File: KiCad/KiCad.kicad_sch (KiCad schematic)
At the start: 48 parts, among them J1 DC-IN, J2 TYPE-C, J3 Conn_01x03_Pin, J4 Conn_01x03_Pin, J5 Conn_01x03_Pin, J6 Conn_01x03_Pin, Q1 IRF3708, SW1 reset, SW2 start, U1 ESP32-WROOM-32E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

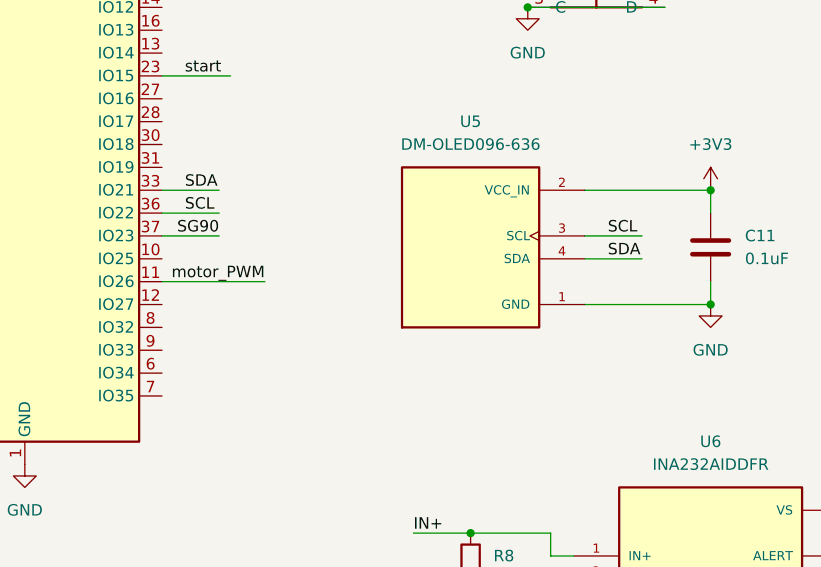
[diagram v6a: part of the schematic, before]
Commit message: 修改iic走線，將原本共用同一組iic的裝置分別接到兩不同的iic
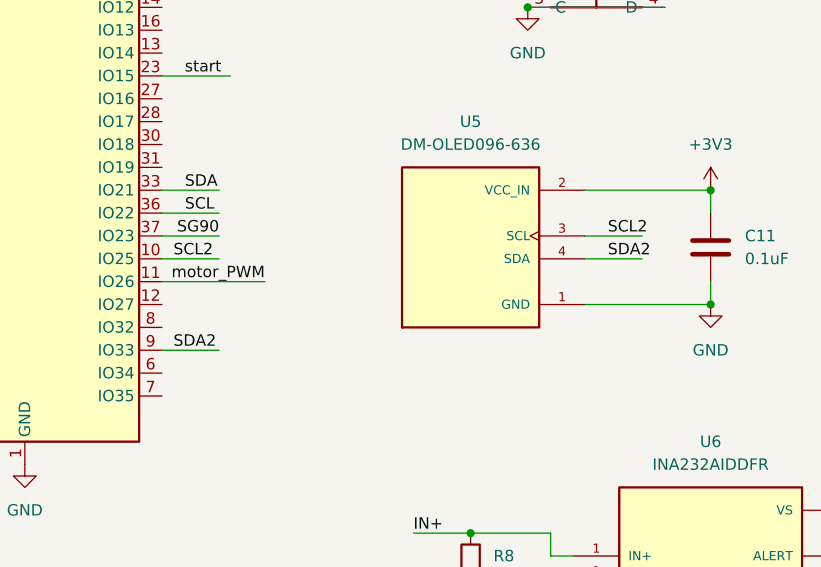
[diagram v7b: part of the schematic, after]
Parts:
- added unit 1 of U8
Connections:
- net SCL: no longer U5.3 (SCL)
- net SDA: no longer U5.4 (SDA)
- net at J6.2 (Pin_2): now also U8.1; no longer U8.1
- net at C17.1, R10.2: now also U8.2 (-), U8.3 (+); no longer U8.2 (-), U8.3 (+)
- net SCL2: now reaches U1.10 (IO25)
- net SCL2: now also U5.3 (SCL)
- net SDA2: now reaches U1.9 (IO33)
- net SDA2: now also U5.4 (SDA)
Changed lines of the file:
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@@
+	(wire
+		(pts
+			(xy 72.39 71.12) (xy 78.74 71.12)
+		)
+		(stroke
+			(width 0)
+			(type default)
+		)
+	)
 	(wire
 		(pts
@@
 	(wire
 		(pts
+			(xy 72.39 81.28) (xy 78.74 81.28)
+		)
+		(stroke
+			(width 0)
+			(type default)
+		)
+	)
+	(wire
+		(pts
 			(xy 261.62 26.67) (xy 266.7 26.67)
 		)
@@
 			(width 0)
 			(type default)
+		)
+	)
+	(label "SDA2"
+		(at 73.66 81.28 0)
+		(effects
+			(font
+				(size 1.27 1.27)
+			)
+			(justify left bottom)
 		)
 	)
@@
 		)
 	)
+	(label "SCL2"
+		(at 73.66 71.12 0)
+		(effects
+			(font
+				(size 1.27 1.27)
+			)
+			(justify left bottom)
+		)
+	)
 	(label "SG90"
 		(at 78.74 68.58 180)
@@
 		)
 	)
-	(label "SDA"
+	(label "SDA2"
 		(at 121.92 71.12 0)
 		(effects
@@
 		)
 	)
-	(label "SCL"
+	(label "SCL2"
 		(at 121.92 68.58 0)
 		(effects

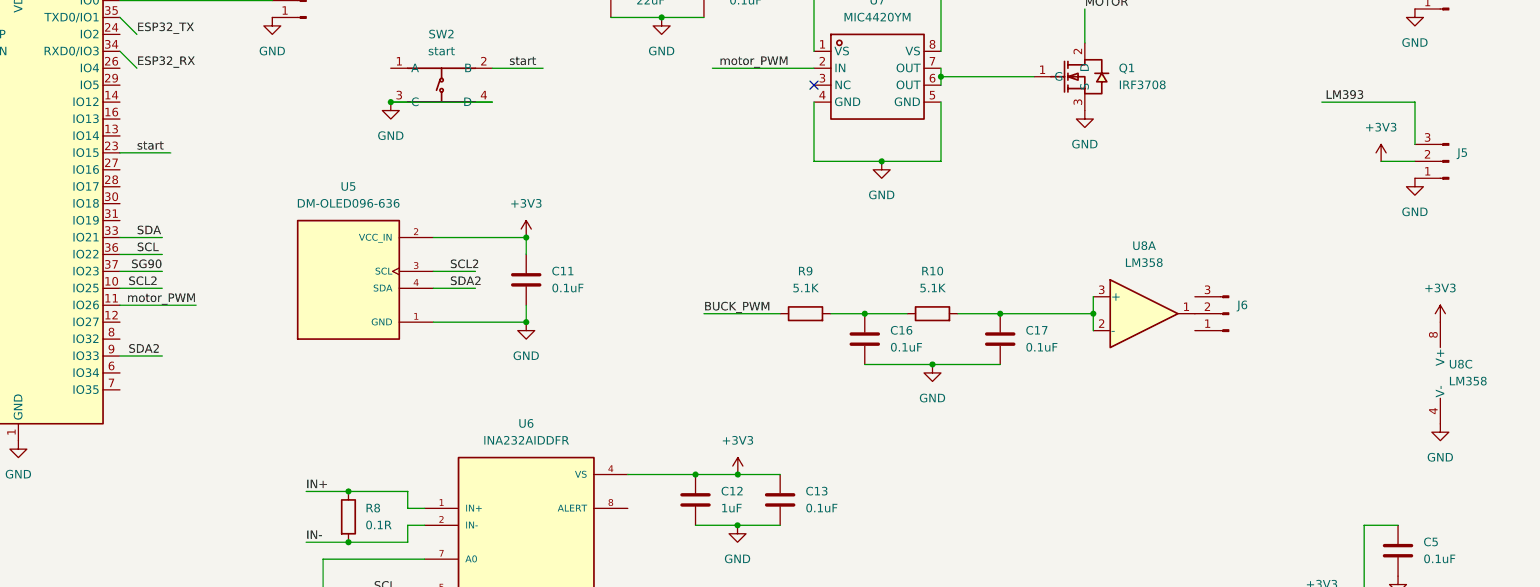
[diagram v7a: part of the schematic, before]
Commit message: 完成PCB及原理圖所有的連接
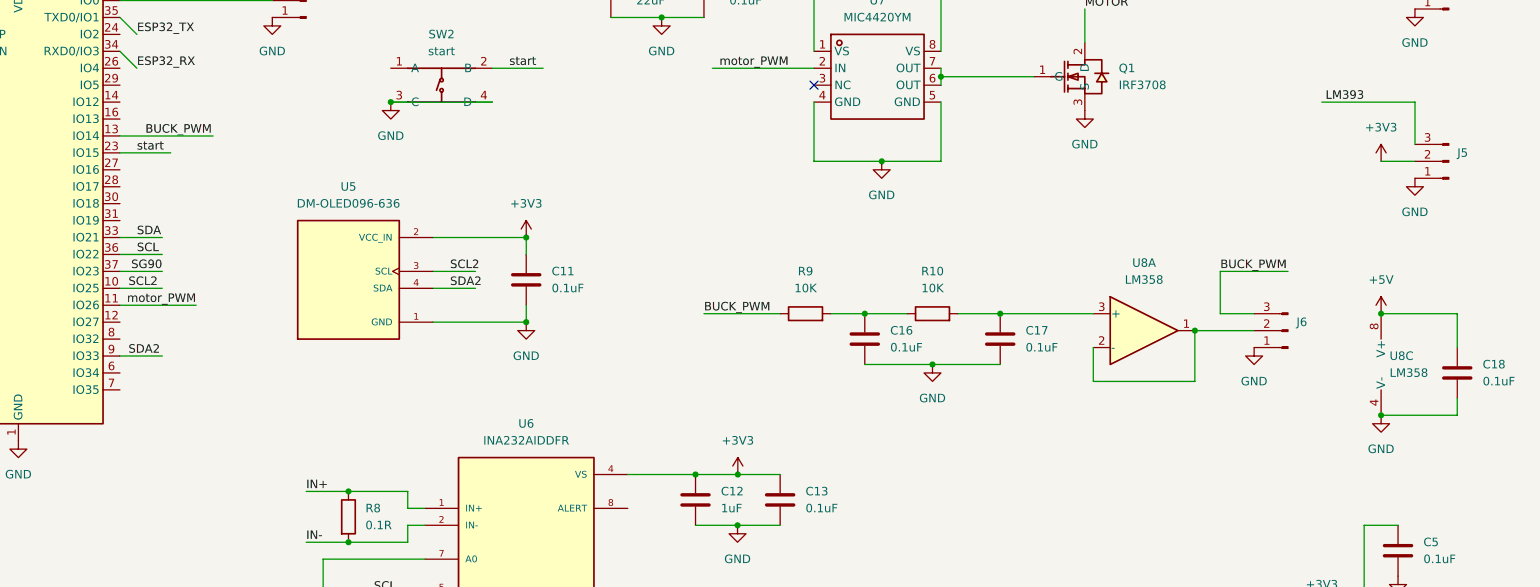
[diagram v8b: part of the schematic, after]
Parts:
- added C18: 0.1uF, Capacitor_SMD:C_0603_1608Metric, symbol Device:C
- R10, R9: value 5.1K -> 10K
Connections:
- net +3V3: no longer U8.8 (V+)
- net +5V: now also U8.8 (V+), C18.1
- net BUCK_PWM: now also J6.3 (Pin_3), U1.13 (IO14)
- net GND: now also J6.1 (Pin_1), C18.2
- net at J6.2 (Pin_2), U8.1: now also U8.2 (-)
- net at C17.1, R10.2, U8.3 (+): no longer U8.2 (-)
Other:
- moved on the sheet: J6, U8A, U8C
